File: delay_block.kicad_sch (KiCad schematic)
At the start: 51 parts, among them J1 Conn_Coaxial, J2 Conn_Coaxial, J3 Conn_Coaxial, J4 Conn_Coaxial, J5 Conn_Coaxial, J6 Conn_Coaxial, J7 Conn_Coaxial, J8 Conn_Coaxial, J9 Screw_Terminal_01x02, U1 DS1100Z-500+, U2 DS1023S-500_, U3 DS1110S-500+, U4 LTC6994CS6-2TRMPBF

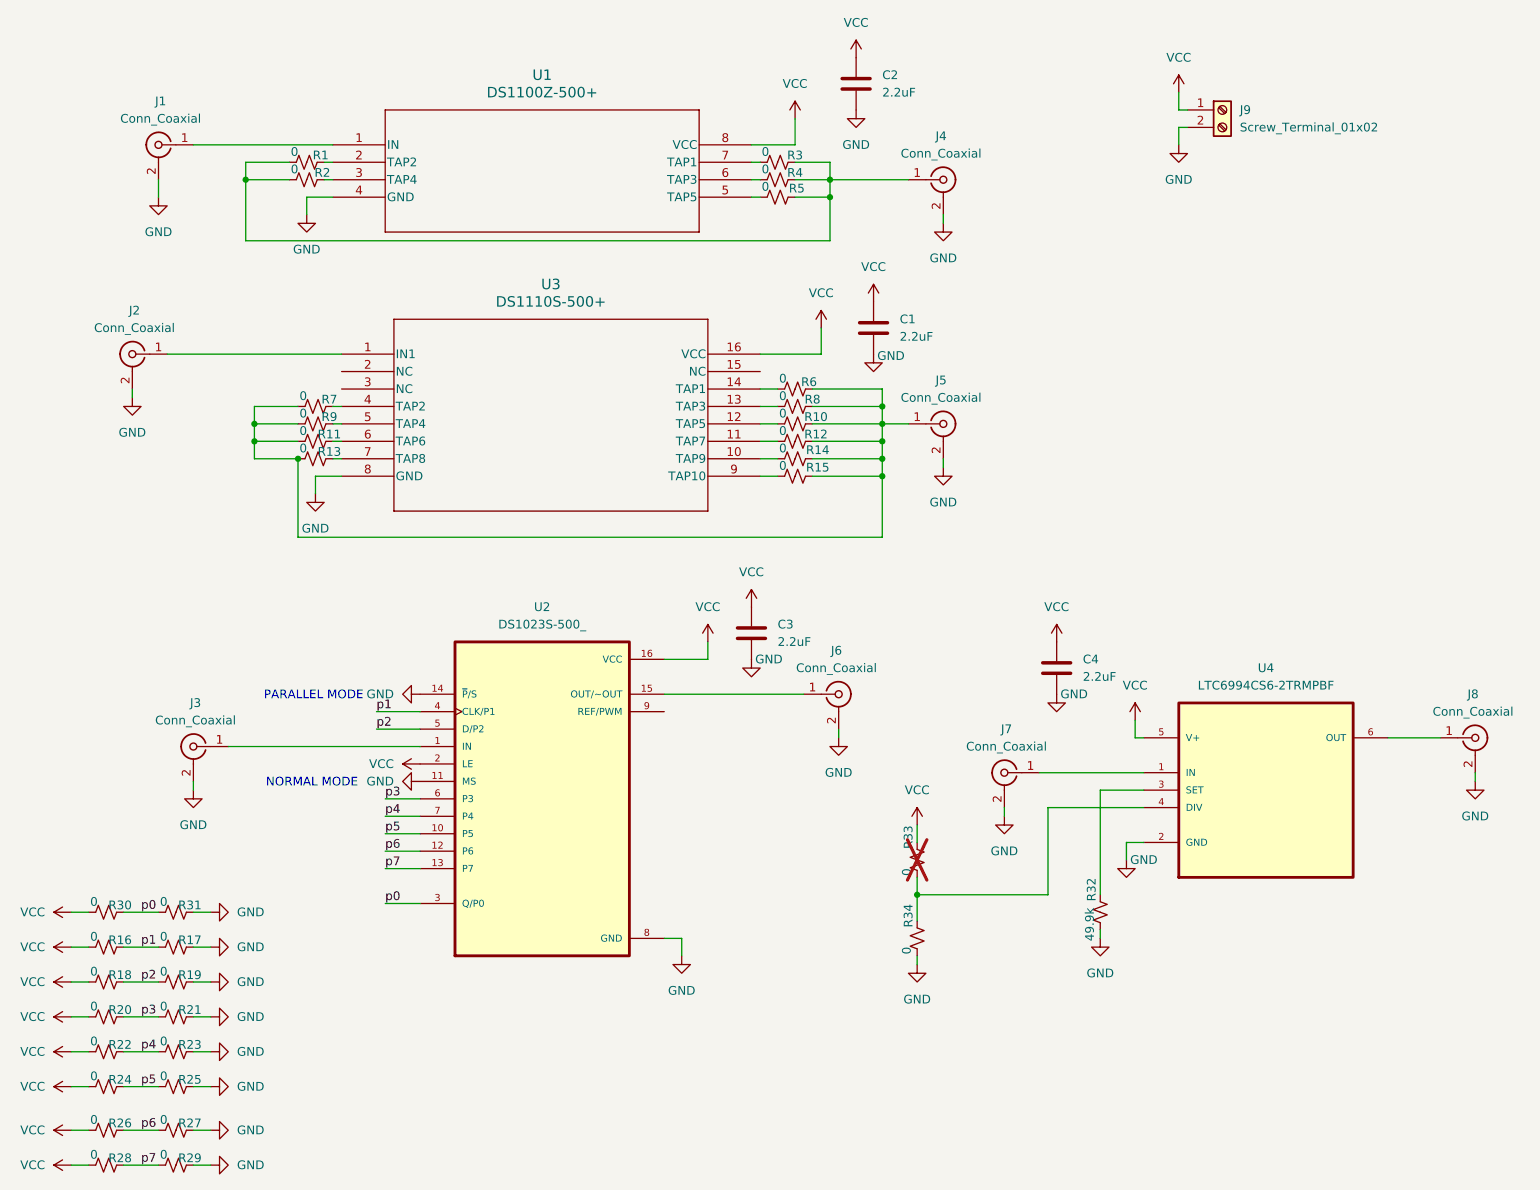
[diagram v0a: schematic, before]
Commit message: Added attributes DNP
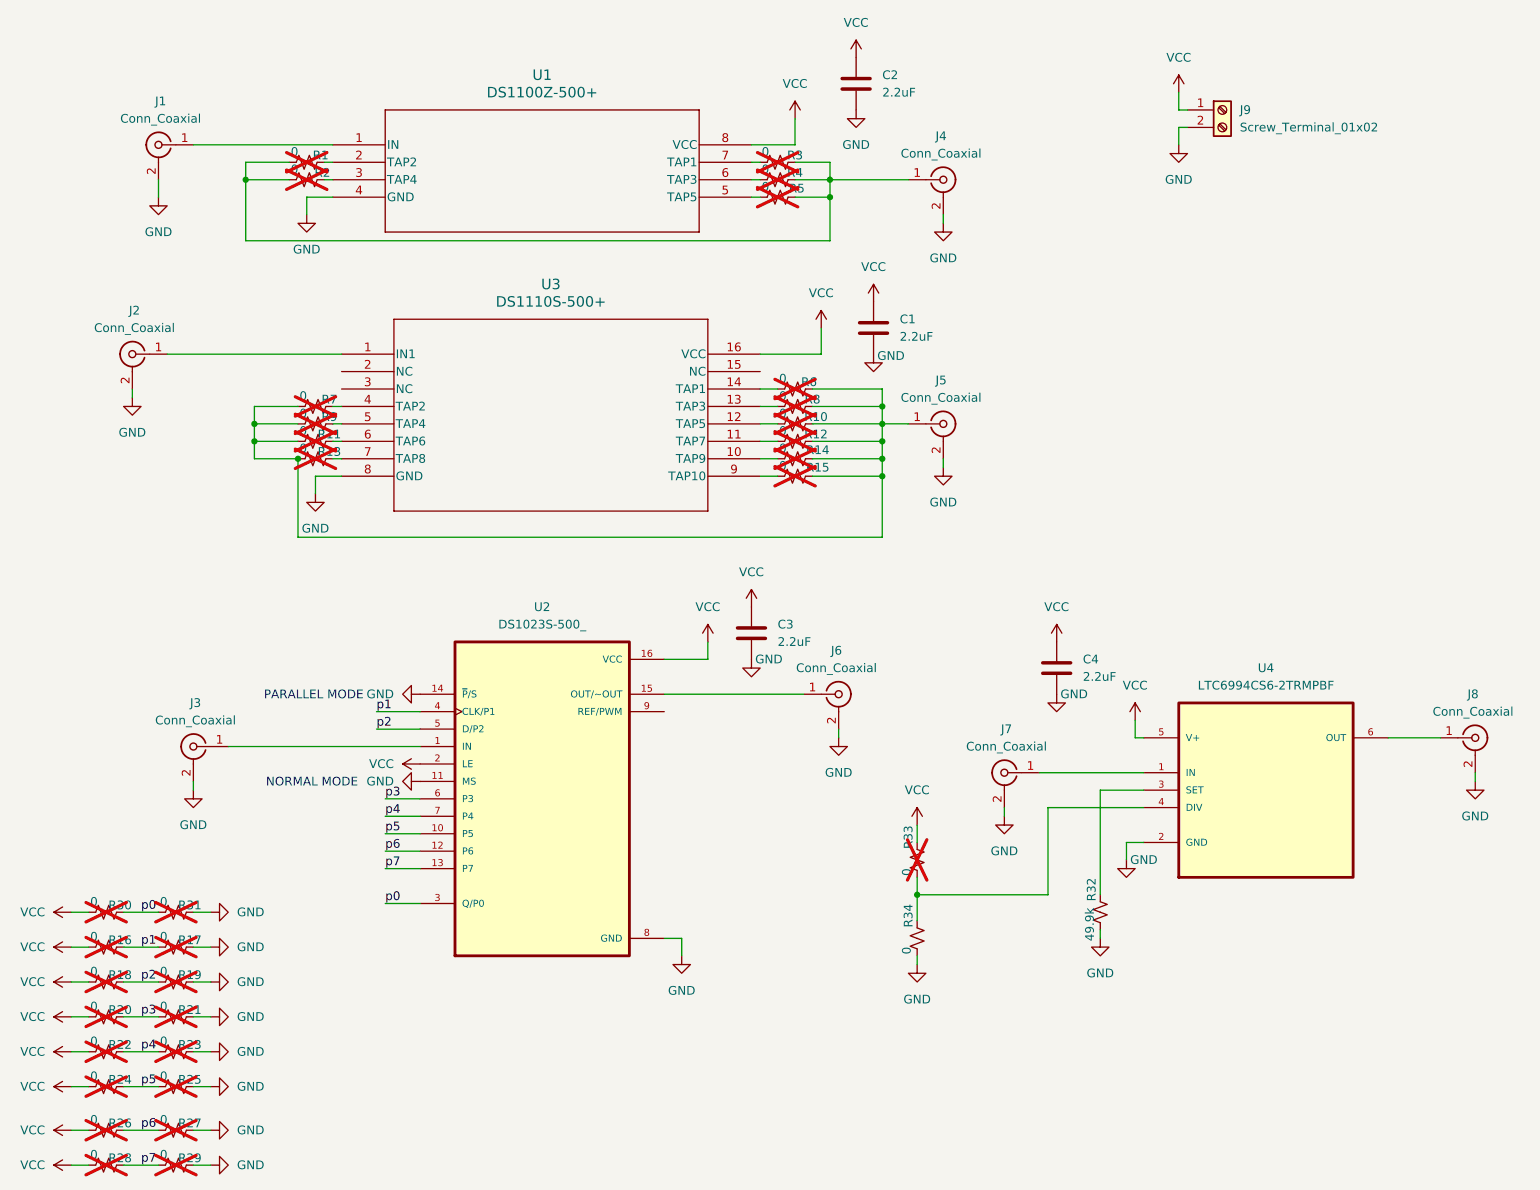
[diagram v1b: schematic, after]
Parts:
- R1, R10, R11, R12, R13, R14, R15, R16, R17, R18, R19, R2, R20, R21, R22, R23, R24, R25, R26, R27, R28, R29, R3, R30, R31, R4, R5, R6, R7, R8, R9: now not fitted
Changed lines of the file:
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@@
 		(in_bom yes)
 		(on_board yes)
-		(dnp no)
+		(dnp yes)
 		(property "Reference" "R17"
 			(at 83.312 151.384 90)
@@
 		(in_bom yes)
 		(on_board yes)
-		(dnp no)
+		(dnp yes)
 		(property "Reference" "R18"
 			(at 73.152 156.464 90)
@@
 		(in_bom yes)
 		(on_board yes)
-		(dnp no)
+		(dnp yes)
 		(property "Reference" "R26"
 			(at 73.152 178.054 90)
@@
 		(in_bom yes)
 		(on_board yes)
-		(dnp no)
+		(dnp yes)
 		(property "Reference" "R15"
 			(at 174.752 82.55 90)
@@
 		(in_bom yes)
 		(on_board yes)
-		(dnp no)
+		(dnp yes)
 		(property "Reference" "R6"
 			(at 173.482 70.104 90)
@@
 		(in_bom yes)
 		(on_board yes)
-		(dnp no)
+		(dnp yes)
 		(property "Reference" "R31"
 			(at 83.312 146.304 90)
@@
 		(in_bom yes)
 		(on_board yes)
-		(dnp no)
+		(dnp yes)
 		(property "Reference" "R21"
 			(at 83.312 161.544 90)
@@
 		(in_bom yes)
 		(on_board yes)
-		(dnp no)
+		(dnp yes)
 		(property "Reference" "R13"
 			(at 103.632 80.264 90)
@@
 		(in_bom yes)
 		(on_board yes)
-		(dnp no)
+		(dnp yes)
 		(property "Reference" "R2"
 			(at 102.616 39.624 90)
@@
 		(in_bom yes)
 		(on_board yes)
-		(dnp no)
+		(dnp yes)
 		(property "Reference" "R24"
 			(at 73.152 171.704 90)
@@
 		(in_bom yes)
 		(on_board yes)
-		(dnp no)
+		(dnp yes)
 		(property "Reference" "R30"
 			(at 73.152 146.304 90)
@@
 		(in_bom yes)
 		(on_board yes)
-		(dnp no)
+		(dnp yes)
 		(property "Reference" "R9"
 			(at 103.632 75.184 90)
@@
 		(in_bom yes)
 		(on_board yes)
-		(dnp no)
+		(dnp yes)
 		(property "Reference" "R12"
 			(at 174.498 77.724 90)
@@
 		(in_bom yes)
 		(on_board yes)
-		(dnp no)
+		(dnp yes)
 		(property "Reference" "R28"
 			(at 73.152 183.134 90)
@@
 		(in_bom yes)
 		(on_board yes)
-		(dnp no)
+		(dnp yes)
 		(property "Reference" "R29"
 			(at 83.312 183.134 90)
@@
 		(in_bom yes)
 		(on_board yes)
-		(dnp no)
+		(dnp yes)
 		(property "Reference" "R20"
 			(at 73.152 161.544 90)
@@
 		(in_bom yes)
 		(on_board yes)
-		(dnp no)
+		(dnp yes)
 		(property "Reference" "R25"
 			(at 83.312 171.704 90)
@@
 		(in_bom yes)
 		(on_board yes)
-		(dnp no)
+		(dnp yes)
 		(property "Reference" "R5"
 			(at 171.704 41.91 90)
@@
 		(in_bom yes)
 		(on_board yes)
-		(dnp no)
+		(dnp yes)
 		(property "Reference" "R7"
 			(at 103.632 72.644 90)
@@
 		(in_bom yes)
 		(on_board yes)
-		(dnp no)
+		(dnp yes)
 		(property "Reference" "R11"
 			(at 103.632 77.724 90)
@@
 		(in_bom yes)
 		(on_board yes)
-		(dnp no)
+		(dnp yes)
 		(property "Reference" "R14"
 			(at 174.752 80.01 90)
@@
 		(in_bom yes)
 		(on_board yes)
-		(dnp no)
+		(dnp yes)
 		(property "Reference" "R4"
 			(at 171.45 39.624 90)
@@
 		(in_bom yes)
 		(on_board yes)
-		(dnp no)
+		(dnp yes)
 		(property "Reference" "R16"
 			(at 73.152 151.384 90)
@@
 		(in_bom yes)
 		(on_board yes)
-		(dnp no)
+		(dnp yes)
 		(property "Reference" "R10"
 			(at 174.498 75.184 90)
@@
 		(in_bom yes)
 		(on_board yes)
-		(dnp no)
+		(dnp yes)
 		(property "Reference" "R22"
 			(at 73.152 166.624 90)
@@
 		(in_bom yes)
 		(on_board yes)
-		(dnp no)
+		(dnp yes)
 		(property "Reference" "R19"
 			(at 83.312 156.464 90)
@@
 		(in_bom yes)
 		(on_board yes)
-		(dnp no)
+		(dnp yes)
 		(property "Reference" "R27"
 			(at 83.312 178.054 90)
@@
 		(in_bom yes)
 		(on_board yes)
-		(dnp no)
+		(dnp yes)
 		(property "Reference" "R3"
 			(at 171.45 37.084 90)
@@
 		(in_bom yes)
 		(on_board yes)
-		(dnp no)
+		(dnp yes)
 		(property "Reference" "R1"
 			(at 102.362 37.084 90)
@@
 		(in_bom yes)
 		(on_board yes)
-		(dnp no)
+		(dnp yes)
 		(property "Reference" "R8"
 			(at 173.99 72.644 90)
@@
 		(in_bom yes)
 		(on_board yes)
-		(dnp no)
+		(dnp yes)
 		(property "Reference" "R23"
 			(at 83.312 166.624 90)
